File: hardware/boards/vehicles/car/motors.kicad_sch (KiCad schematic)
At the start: 43 parts, among them J9 Conn_02x05_Odd_Even, M1 Motor_DC, M2 Motor_DC, Q1 FQP27P06, Q10 AO3400A, Q11 2N3904, Q12 2N3904, Q2 AO3400A, Q3 FQP27P06, Q4 AO3400A, Q5 2N3904, Q6 2N3904, Q7 FQP27P06, Q8 AO3400A, Q9 FQP27P06

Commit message: REFACTO relinked every kicad projects
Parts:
- D10, D11, D4, D5, D6, D7, D8, D9: footprint Diode_SMD:D_SMA_Handsoldering -> Diode_THT:D_DO-201AD_P15.24mm_Horizontal
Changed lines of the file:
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@@
 			)
 		)
-		(property "Footprint" "Diode_SMD:D_SMA_Handsoldering"
+		(property "Footprint" "Diode_THT:D_DO-201AD_P15.24mm_Horizontal"
 			(at 189.23 102.235 0)
 			(effects
@@
 			)
 		)
-		(property "Datasheet" ""
+		(property "Datasheet" "http://www.vishay.com/docs/88756/uf5400.pdf"
 			(at 189.23 97.79 0)
 			(effects
@@
 			)
 		)
-		(property "Description" ""
+		(property "Description" "1000V 3A Soft Recovery Ultrafast Rectifier Diode, DO-201AD"
 			(at 189.23 97.79 0)
 			(effects
@@
 			)
 		)
-		(property "Footprint" "Diode_SMD:D_SMA_Handsoldering"
+		(property "Footprint" "Diode_THT:D_DO-201AD_P15.24mm_Horizontal"
 			(at 204.47 102.235 0)
 			(effects
@@
 			)
 		)
-		(property "Datasheet" ""
+		(property "Datasheet" "http://www.vishay.com/docs/88756/uf5400.pdf"
 			(at 204.47 97.79 0)
 			(effects
@@
 			)
 		)
-		(property "Description" ""
+		(property "Description" "1000V 3A Soft Recovery Ultrafast Rectifier Diode, DO-201AD"
 			(at 204.47 97.79 0)
 			(effects
@@
 			)
 		)
+		(property "Sim.Device" "NPN"
+			(at 91.44 72.39 0)
+			(effects
+				(font
+					(size 1.27 1.27)
+				)
+				(hide yes)
+			)
+		)
+		(property "Sim.Pins" "1=E 2=B 3=C"
+			(at 91.44 72.39 0)
+			(effects
+				(font
+					(size 1.27 1.27)
+				)
+				(hide yes)
+			)
+		)
 		(pin "2"
 		)
@@
 			)
 		)
-		(property "Footprint" "Diode_SMD:D_SMA_Handsoldering"
+		(property "Footprint" "Diode_THT:D_DO-201AD_P15.24mm_Horizontal"
 			(at 87.63 102.235 0)
 			(effects
@@
 			)
 		)
-		(property "Datasheet" ""
+		(property "Datasheet" "http://www.vishay.com/docs/88756/uf5400.pdf"
 			(at 87.63 97.79 0)
 			(effects
@@
 			)
 		)
-		(property "Description" ""
+		(property "Description" "1000V 3A Soft Recovery Ultrafast Rectifier Diode, DO-201AD"
 			(at 87.63 97.79 0)
 			(effects
@@
 		)
 		(property "Description" "0.2A Ic, 40V Vce, Small Signal NPN Transistor, TO-92"
+			(at 91.44 143.51 0)
+			(effects
+				(font
+					(size 1.27 1.27)
+				)
+				(hide yes)
+			)
+		)
+		(property "Sim.Device" "NPN"
+			(at 91.44 143.51 0)
+			(effects
+				(font
+					(size 1.27 1.27)
+				)
+				(hide yes)
+			)
+		)
+		(property "Sim.Pins" "1=E 2=B 3=C"
 			(at 91.44 143.51 0)
 			(effects
@@
 			)
 		)
-		(property "Footprint" "Diode_SMD:D_SMA_Handsoldering"
+		(property "Footprint" "Diode_THT:D_DO-201AD_P15.24mm_Horizontal"
 			(at 189.23 122.555 0)
 			(effects
@@
 			)
 		)
-		(property "Datasheet" ""
+		(property "Datasheet" "http://www.vishay.com/docs/88756/uf5400.pdf"
 			(at 189.23 118.11 0)
 			(effects
@@
 			)
 		)
-		(property "Description" ""
+		(property "Description" "1000V 3A Soft Recovery Ultrafast Rectifier Diode, DO-201AD"
 			(at 189.23 118.11 0)
 			(effects
@@
 			)
 		)
-		(property "Footprint" "Diode_SMD:D_SMA_Handsoldering"
+		(property "Footprint" "Diode_THT:D_DO-201AD_P15.24mm_Horizontal"
 			(at 102.87 102.235 0)
 			(effects
@@
 			)
 		)
-		(property "Datasheet" ""
+		(property "Datasheet" "http://www.vishay.com/docs/88756/uf5400.pdf"
 			(at 102.87 97.79 0)
 			(effects
@@
 			)
 		)
-		(property "Description" ""
+		(property "Description" "1000V 3A Soft Recovery Ultrafast Rectifier Diode, DO-201AD"
 			(at 102.87 97.79 0)
 			(effects
@@
 			)
 		)
+		(property "Sim.Device" "NPN"
+			(at 193.04 143.51 0)
+			(effects
+				(font
+					(size 1.27 1.27)
+				)
+				(hide yes)
+			)
+		)
+		(property "Sim.Pins" "1=E 2=B 3=C"
+			(at 193.04 143.51 0)
+			(effects
+				(font
+					(size 1.27 1.27)
+				)
+				(hide yes)
+			)
+		)
 		(pin "2"
 		)
@@
 			)
 		)
-		(property "Footprint" "Diode_SMD:D_SMA_Handsoldering"
+		(property "Footprint" "Diode_THT:D_DO-201AD_P15.24mm_Horizontal"
 			(at 87.63 122.555 0)
 			(effects
@@
 			)
 		)
-		(property "Datasheet" ""
+		(property "Datasheet" "http://www.vishay.com/docs/88756/uf5400.pdf"
 			(at 87.63 118.11 0)
 			(effects
@@
 			)
 		)
-		(property "Description" ""
+		(property "Description" "1000V 3A Soft Recovery Ultrafast Rectifier Diode, DO-201AD"
 			(at 87.63 118.11 0)
 			(effects
@@
 			)
 		)
-		(property "Footprint" "Diode_SMD:D_SMA_Handsoldering"
+		(property "Footprint" "Diode_THT:D_DO-201AD_P15.24mm_Horizontal"
 			(at 102.87 122.555 0)
 			(effects
@@
 			)
 		)
-		(property "Datasheet" ""
+		(property "Datasheet" "http://www.vishay.com/docs/88756/uf5400.pdf"
 			(at 102.87 118.11 0)
 			(effects
@@
 			)
 		)
-		(property "Description" ""
+		(property "Description" "1000V 3A Soft Recovery Ultrafast Rectifier Diode, DO-201AD"
 			(at 102.87 118.11 0)
 			(effects
@@
 			)
 		)
-		(property "Footprint" "Diode_SMD:D_SMA_Handsoldering"
+		(property "Footprint" "Diode_THT:D_DO-201AD_P15.24mm_Horizontal"
 			(at 204.47 122.555 0)
 			(effects
@@
 			)
 		)
-		(property "Datasheet" ""
+		(property "Datasheet" "http://www.vishay.com/docs/88756/uf5400.pdf"
 			(at 204.47 118.11 0)
 			(effects
@@
 			)
 		)
-		(property "Description" ""
+		(property "Description" "1000V 3A Soft Recovery Ultrafast Rectifier Diode, DO-201AD"
 			(at 204.47 118.11 0)
 			(effects
@@
 			(at 193.04 72.39 0)
 			(effects
+				(font
+					(size 1.27 1.27)
+				)
+				(hide yes)
+			)
+		)
+		(property "Sim.Device" "NPN"
+			(at 193.04 72.39 0)
+			(effects
+				(font
+					(size 1.27 1.27)
+				)
+				(hide yes)
+			)
+		)
+		(property "Sim.Pins" "1=E 2=B 3=C"
+			(at 193.04 72.39 0)
+			(effects

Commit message: car PCB
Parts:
- removed J9: Conn_02x05_Odd_Even, Connector_PinHeader_2.54mm:PinHeader_2x05_P2.54mm_Vertical, symbol Connector_Generic:Conn_02x05_Odd_Even
- C20: renamed from C13; footprint Capacitor_THT:CP_Radial_D10.0mm_P5.00mm -> common:CP_Elec_8x10.5
- C22: renamed from C15; footprint Capacitor_THT:CP_Radial_D10.0mm_P5.00mm -> common:CP_Elec_8x10.5
- D10: renamed from D9; footprint Diode_THT:D_DO-201AD_P15.24mm_Horizontal -> common:SMA(DO-214AC)
- D11: renamed from D10; footprint Diode_THT:D_DO-201AD_P15.24mm_Horizontal -> common:SMA(DO-214AC)
- D12: renamed from D11; footprint Diode_THT:D_DO-201AD_P15.24mm_Horizontal -> common:SMA(DO-214AC)
- D5: renamed from D4; footprint Diode_THT:D_DO-201AD_P15.24mm_Horizontal -> common:SMA(DO-214AC)
- D6: renamed from D5; footprint Diode_THT:D_DO-201AD_P15.24mm_Horizontal -> common:SMA(DO-214AC)
- D7: renamed from D6; footprint Diode_THT:D_DO-201AD_P15.24mm_Horizontal -> common:SMA(DO-214AC)
- D8: renamed from D7; footprint Diode_THT:D_DO-201AD_P15.24mm_Horizontal -> common:SMA(DO-214AC)
- D9: renamed from D8; footprint Diode_THT:D_DO-201AD_P15.24mm_Horizontal -> common:SMA(DO-214AC)
- M1: value Motor_DC -> LEFT; footprint Connector_PinHeader_2.54mm:PinHeader_1x02_P2.54mm_Vertical -> Connector_JST:JST_XH_B2B-XH-A_1x02_P2.50mm_Vertical
- M2: value Motor_DC -> RIGHT; footprint Connector_PinHeader_2.54mm:PinHeader_1x02_P2.54mm_Vertical -> Connector_JST:JST_XH_B2B-XH-A_1x02_P2.50mm_Vertical
- renumbered C14 to C21, C16 to C23, Q3 to Q2, Q2 to Q3, Q9 to Q8, Q8 to Q9, R7 to R15, R14 to R16, R8 to R17, R13 to R18, R9 to R19, R12 to R20, R10 to R21, R11 to R22, R15 to R23, R22 to R24, R16 to R25, R21 to R26, R17 to R27, R20 to R28, R18 to R29, R19 to R30

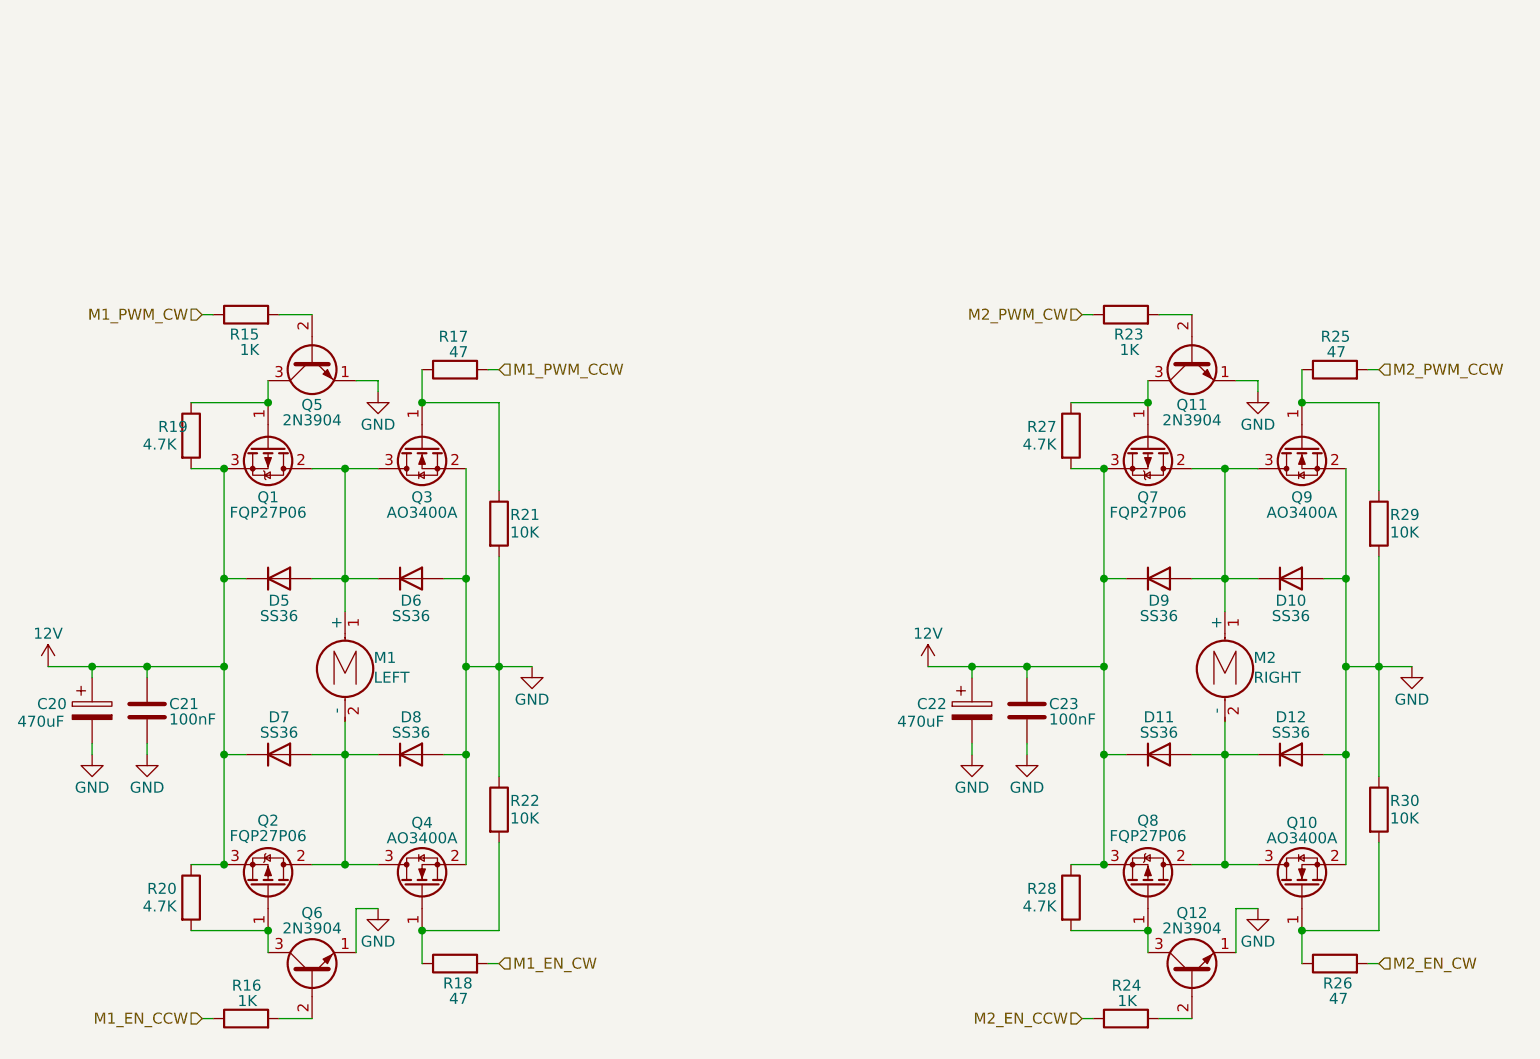
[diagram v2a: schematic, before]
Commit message: change kicad default to custom
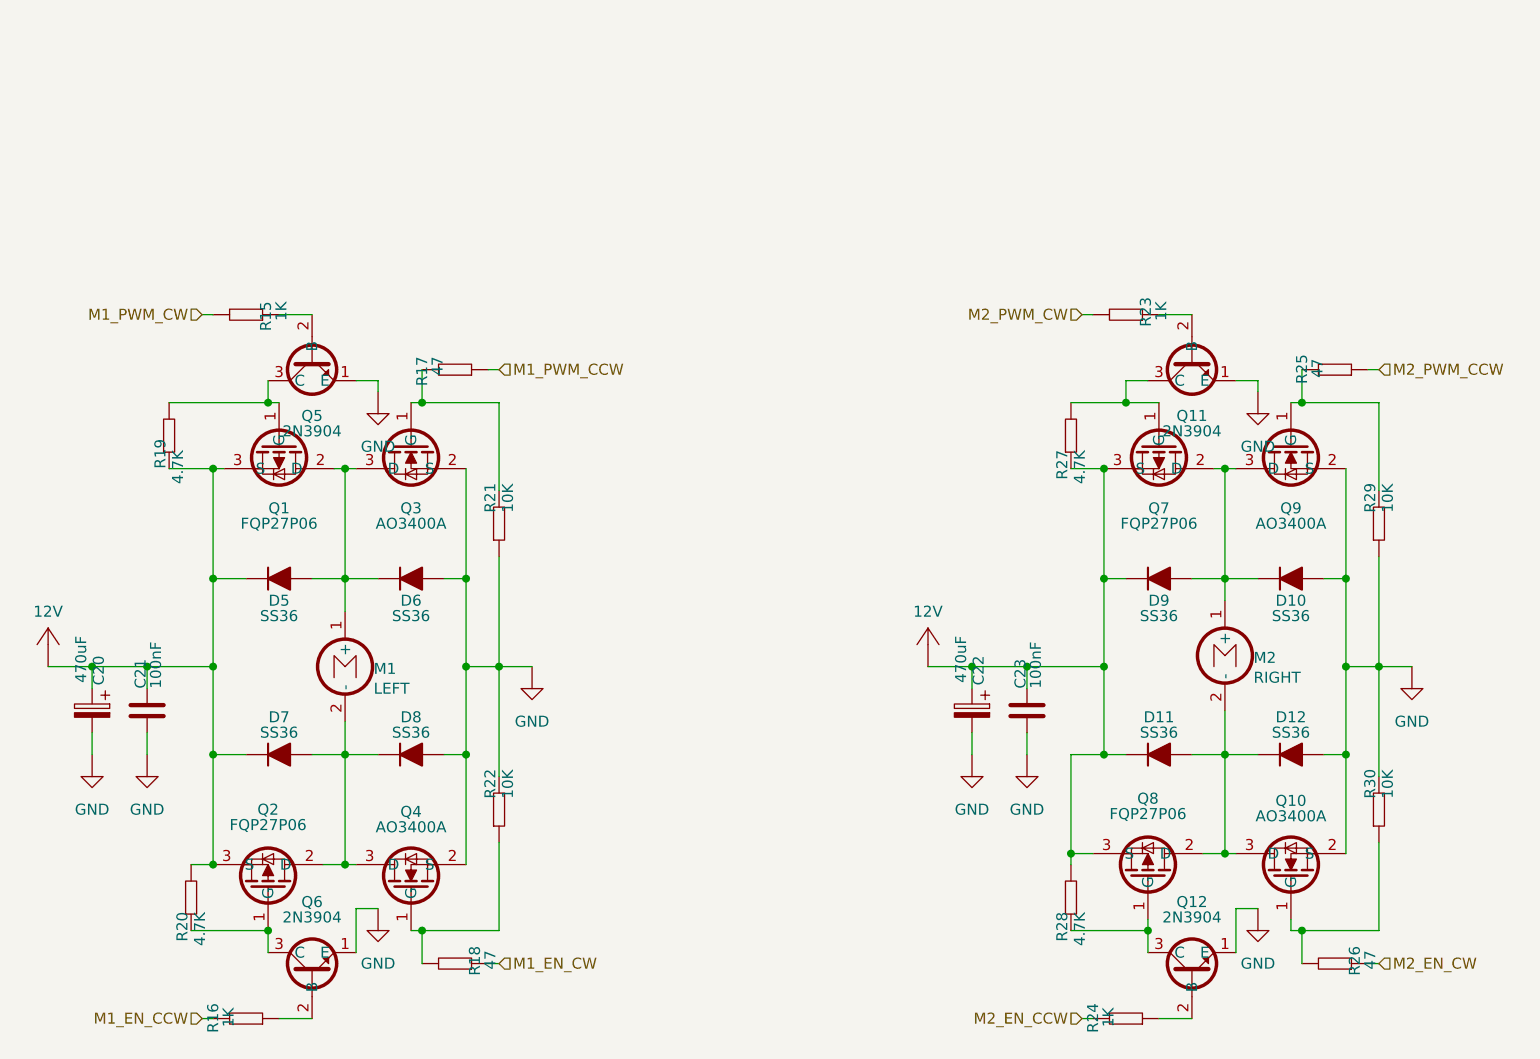
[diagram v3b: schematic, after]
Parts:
- C20, C22: symbol Device:C_Polarized -> common:Capacitor_Electrolytic
- C21, C23: footprint Capacitor_SMD:C_0603_1608Metric_Pad1.08x0.95mm_HandSolder -> common:C_0603; symbol Device:C -> common:Capacitor
- D10, D11, D12, D5, D6, D7, D8, D9: symbol Diode:UF5408 -> common:Diode
- M1, M2: footprint Connector_JST:JST_XH_B2B-XH-A_1x02_P2.50mm_Vertical -> connector:JST_1x2; symbol Motor:Motor_DC -> misc:Motor_DC
- Q1, Q2, Q7, Q8: symbol Transistor_FET:FQP27P06 -> transistor:FQP27P06
- Q10, Q3, Q4, Q9: symbol Transistor_FET:AO3400A -> transistor:AO3400A
- Q11, Q12, Q5, Q6: footprint Package_TO_SOT_THT:TO-92_Inline -> transistor:2N3903_TO-92; symbol Transistor_BJT:2N3904 -> transistor:2N3904
- R15, R16, R17, R18, R19, R20, R21, R22, R23, R24, R25, R26, R27, R28, R29, R30: footprint Resistor_SMD:R_0603_1608Metric_Pad0.98x0.95mm_HandSolder -> common:R_0603; symbol Device:R -> common:Resistor
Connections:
- net 12V: now also C21.2, C23.2, R19.1, R20.2, R27.1, R28.2; no longer C21.1, C23.1, R19.2, R20.1, R27.2, R28.1
- net GND: now also C21.1, C23.1, R21.1, R22.2, R29.1, R30.2; no longer C21.2, C23.2, R21.2, R22.1, R29.2, R30.1
- net M1_EN_CCW: now also R16.2; no longer R16.1
- net M1_EN_CW: now also R18.1; no longer R18.2
- net M1_PWM_CCW: now also R17.1; no longer R17.2
- net M1_PWM_CW: now also R15.2; no longer R15.1
- net M2_EN_CCW: now also R24.2; no longer R24.1
- net M2_EN_CW: now also R26.1; no longer R26.2
- net M2_PWM_CCW: now also R25.1; no longer R25.2
- net M2_PWM_CW: now also R23.2; no longer R23.1
- net at Q6.2 (B): now also R16.1; no longer R16.2
- net at Q5.2 (B): now also R15.1; no longer R15.2
- net at Q1.1 (G), Q5.3 (C): now also R19.2; no longer R19.1
- net at Q12.3 (C), Q8.1 (G): now also R28.1; no longer R28.2
- net at Q11.2 (B): now also R23.1; no longer R23.2
- net at Q2.1 (G), Q6.3 (C): now also R20.1; no longer R20.2
- net at Q12.2 (B): now also R24.1; no longer R24.2
- net at Q11.3 (C), Q7.1 (G): now also R27.2; no longer R27.1
- new net: Q9.1 (G), R25.2, R29.2
- new net: Q3.1 (G), R17.2, R21.2
- new net: Q4.1 (G), R18.2, R22.1
- new net: Q10.1 (G), R26.2, R30.1
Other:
- moved on the sheet: C20, C21, C22, C23, Q1, Q10, Q3, Q4, Q7, Q8, Q9, R15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
